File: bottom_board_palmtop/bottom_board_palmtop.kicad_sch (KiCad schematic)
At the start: 80 parts, among them J4 FFC_2, J44 PROGesterone, J5 FFC_1, J50 SH 4P, J6 SH 4P, U21 XL9535QF24, U22 TPAZ1043-04F, U23 TPAZ1043-04F, U28 XL9535QF24, U41 TPAZ1043-04F, U5 W25Q16JV, U6 RP2040, Y1 12MHz

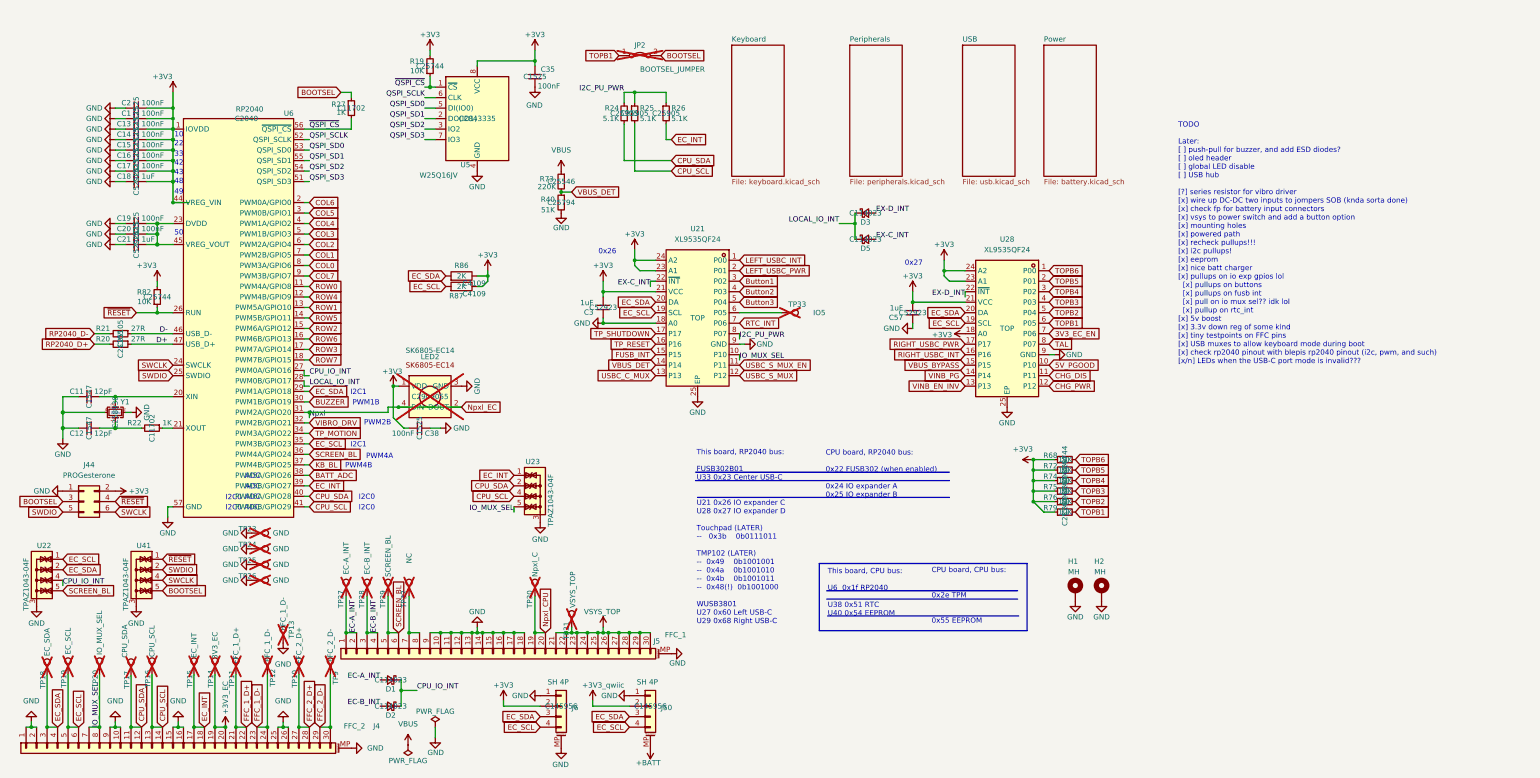
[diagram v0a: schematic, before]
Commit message: bottom_board_palmtop: JLC PCBA preparation; clarifying I2C addresses in use
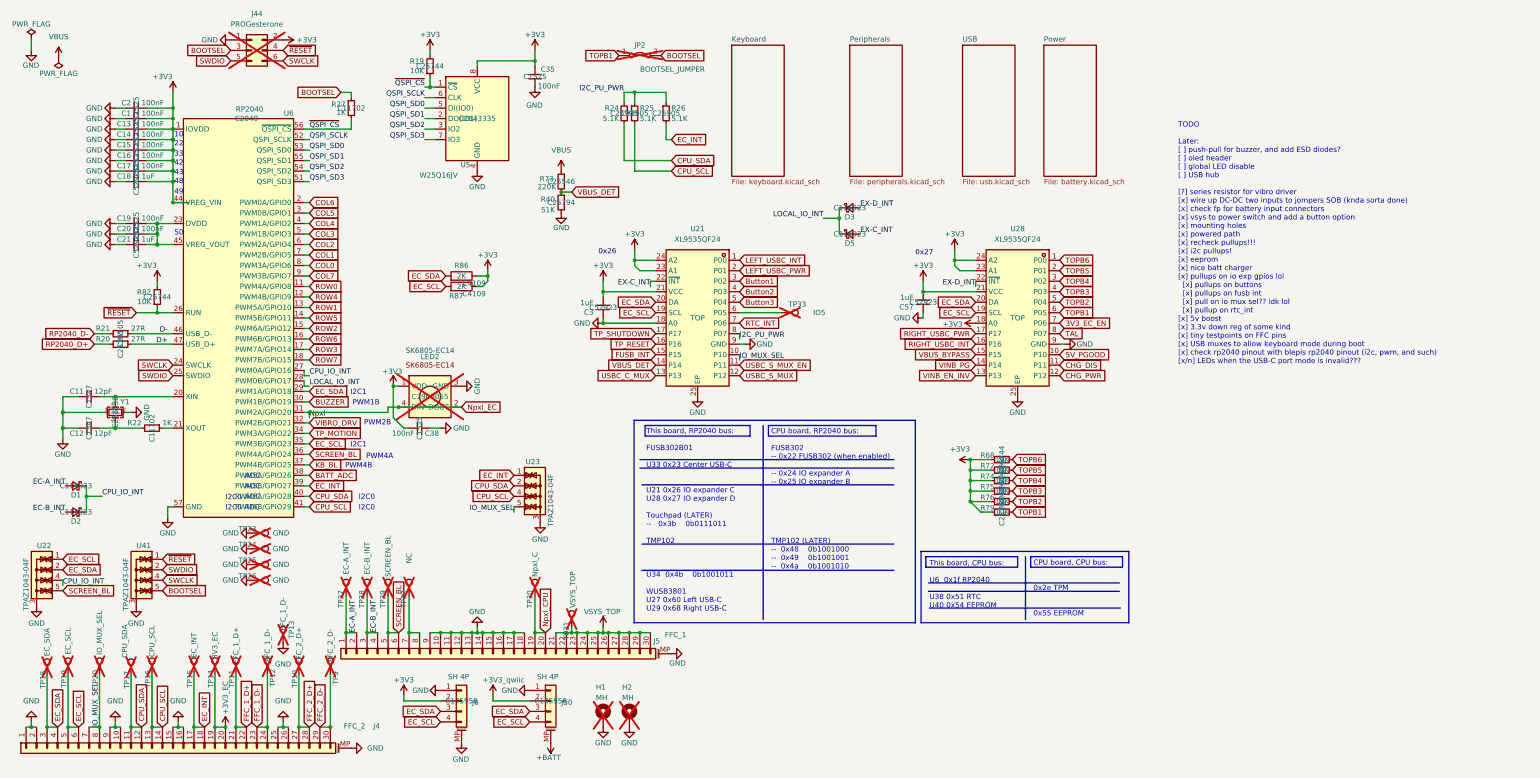
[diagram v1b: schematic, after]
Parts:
- H1, H2, J44: now not fitted
- JP2: now left out of the parts list
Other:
- note added: "CPU board, RP2040 bus: FUSB302 -- 0x22 FUSB302 (when enabled) -- 0x24 IO expander A -- 0x25 IO expander B TMP102 (LATER) -- 0x48 0b1001000 -- 0x49 0b1001001 -- 0x4a 0b1001010"
- note added: "This board, RP2040 bus: FUSB302B01 U33 0x23 Center USB-C U21 0x26 IO expander C U28 0x27 IO expander D Touchpad (LATER) -- 0x3b 0b0111011 TMP102 U34 0x4b 0b1001011 WUSB3801 U27 0x60 Left USB-C U29 0x68 Right USB-C"
- note removed: "CPU board, RP2040 bus: 0x22 FUSB302 (when enabled) 0x24 IO expander A 0x25 IO expander B"
- note removed: "This board, RP2040 bus: FUSB302B01 U33 0x23 Center USB-C U21 0x26 IO expander C U28 0x27 IO expander D Touchpad (LATER) -- 0x3b 0b0111011 TMP102 (LATER) -- 0x49 0b1001001 -- 0x4a 0b1001010 -- 0x4b 0b1001011 -- 0x48(!) 0b1001000 WUSB3801 U27 0x60 Left USB-C U29 0x68 Right USB-C"
- moved on the sheet: C57, D1, D2, D3, D5, J50, J6, R68, R72, R74, R75, R76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
